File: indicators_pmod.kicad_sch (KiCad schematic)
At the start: 21 parts, among them IC1 ECP5-BGA256

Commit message: rename libraries from luna to cynthion
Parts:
- IC1: footprint luna:lattice_cabga256 -> cynthion:lattice_cabga256
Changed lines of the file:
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@@
       (effects (font (size 1.27 1.27)) (justify right))
     )
-    (property "Footprint" "luna:lattice_cabga256" (id 2) (at -31.75 -35.56 0)
+    (property "Footprint" "cynthion:lattice_cabga256" (id 2) (at -31.75 -35.56 0)
       (effects (font (size 1.27 1.27)) (justify left) hide)
     )

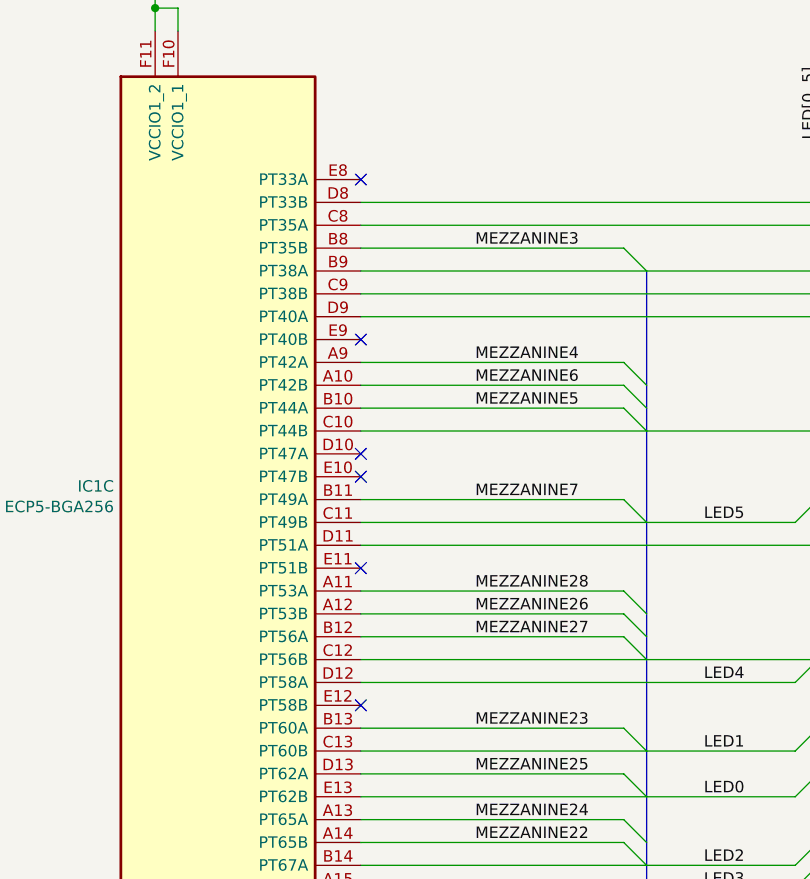
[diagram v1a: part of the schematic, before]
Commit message: Add pseudo-VCCIO and pseudo-GND pins, decoupling
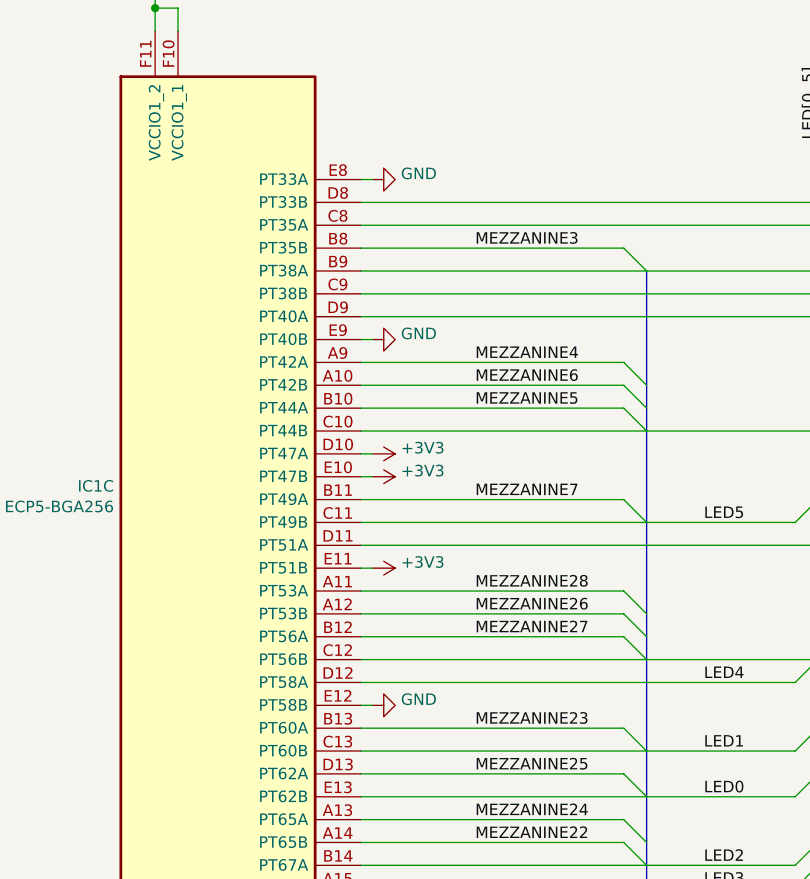
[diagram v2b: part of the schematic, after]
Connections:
- net +3V3: now also IC1.D10 (PT47A), IC1.E10 (PT47B), IC1.E11 (PT51B)
- net GND: now reaches IC1.E12 (PT58B)
- net GND: now also IC1.E8 (PT33A), IC1.E9 (PT40B)
- no-connect marks 6 -> 0
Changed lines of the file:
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@@
   (junction (at 151.765 58.42) (diameter 0) (color 0 0 0 0)
   )
-  (no_connect (at 76.2 93.98))
-  (no_connect (at 76.2 81.28))
-  (no_connect (at 76.2 63.5))
-  (no_connect (at 76.2 106.68))
-  (no_connect (at 76.2 96.52))
-  (no_connect (at 76.2 121.92))
   (bus_entry (at 127 139.7) (size -2.54 2.54)
     (stroke (width 0) (type default) (color 0 0 0 0))
@@
     (stroke (width 0) (type default) (color 0 0 0 0))
   )
+  (wire (pts (xy 76.2 81.28) (xy 77.47 81.28))
+    (stroke (width 0) (type default) (color 0 0 0 0))
+  )
   (wire (pts (xy 129.54 50.8) (xy 139.7 50.8))
     (stroke (width 0) (type default) (color 0 0 0 0))
@@
     (stroke (width 0) (type default) (color 0 0 0 0))
   )
+  (wire (pts (xy 76.2 63.5) (xy 77.47 63.5))
+    (stroke (width 0) (type default) (color 0 0 0 0))
+  )
   (wire (pts (xy 76.2 137.16) (xy 105.41 137.16))
     (stroke (width 0) (type default) (color 0 0 0 0))
   )
+  (wire (pts (xy 77.47 96.52) (xy 76.2 96.52))
+    (stroke (width 0) (type default) (color 0 0 0 0))
+  )
   (wire (pts (xy 177.165 50.8) (xy 179.705 50.8))
     (stroke (width 0) (type default) (color 0 0 0 0))
@@
     (stroke (width 0) (type default) (color 0 0 0 0))
   )
+  (wire (pts (xy 77.47 93.98) (xy 76.2 93.98))
+    (stroke (width 0) (type default) (color 0 0 0 0))
+  )
   (bus (pts (xy 127 60.96) (xy 127 99.06))
     (stroke (width 0) (type default) (color 0 0 0 0))
@@
     (stroke (width 0) (type default) (color 0 0 0 0))
   )
+  (wire (pts (xy 76.2 121.92) (xy 77.47 121.92))
+    (stroke (width 0) (type default) (color 0 0 0 0))
+  )
   (bus (pts (xy 217.17 90.17) (xy 217.17 92.71))
     (stroke (width 0) (type default) (color 0 0 0 0))
@@
   )
   (wire (pts (xy 147.32 55.88) (xy 153.035 55.88))
+    (stroke (width 0) (type default) (color 0 0 0 0))
+  )
+  (wire (pts (xy 76.2 106.68) (xy 77.47 106.68))
     (stroke (width 0) (type default) (color 0 0 0 0))
   )
@@
     )
     (property "Datasheet" "~" (id 3) (at 147.955 37.465 0)
+      (effects (font (size 1.27 1.27)) hide)
+    )
+    (pin "1")
+  )
+  (symbol (lib_id "power:GND") (at 77.47 121.92 90) (unit 1)
+    (in_bom yes) (on_board yes)
+    (property "Reference" "#PWR0232" (id 0) (at 83.82 121.92 0)
+      (effects (font (size 1.27 1.27)) hide)
+    )
+    (property "Value" "GND" (id 1) (at 80.645 121.285 90)
+      (effects (font (size 1.27 1.27)) (justify right))
+    )
+    (property "Footprint" "" (id 2) (at 77.47 121.92 0)
+      (effects (font (size 1.27 1.27)) hide)
+    )
+    (property "Datasheet" "" (id 3) (at 77.47 121.92 0)
       (effects (font (size 1.27 1.27)) hide)
     )
@@
     (pin "1")
   )
+  (symbol (lib_id "power:GND") (at 77.47 63.5 90) (unit 1)
+    (in_bom yes) (on_board yes)
+    (property "Reference" "#PWR0227" (id 0) (at 83.82 63.5 0)
+      (effects (font (size 1.27 1.27)) hide)
+    )
+    (property "Value" "GND" (id 1) (at 80.645 62.865 90)
+      (effects (font (size 1.27 1.27)) (justify right))
+    )
+    (property "Footprint" "" (id 2) (at 77.47 63.5 0)
+      (effects (font (size 1.27 1.27)) hide)
+    )
+    (property "Datasheet" "" (id 3) (at 77.47 63.5 0)
+      (effects (font (size 1.27 1.27)) hide)
+    )
+    (pin "1")
+  )
+  (symbol (lib_id "power:GND") (at 77.47 81.28 90) (unit 1)
+    (in_bom yes) (on_board yes)
+    (property "Reference" "#PWR0228" (id 0) (at 83.82 81.28 0)
+      (effects (font (size 1.27 1.27)) hide)
+    )
+    (property "Value" "GND" (id 1) (at 80.645 80.645 90)
+      (effects (font (size 1.27 1.27)) (justify right))
+    )
+    (property "Footprint" "" (id 2) (at 77.47 81.28 0)
+      (effects (font (size 1.27 1.27)) hide)
+    )
+    (property "Datasheet" "" (id 3) (at 77.47 81.28 0)
+      (effects (font (size 1.27 1.27)) hide)
+    )
+    (pin "1")
+  )
   (symbol (lib_id "Connector:TestPoint") (at 154.305 33.02 0) (mirror y) (unit 1)
     (in_bom no) (on_board yes)
@@
     (pin "8")
   )
+  (symbol (lib_id "power:+3V3") (at 77.47 96.52 270) (unit 1)
+    (in_bom yes) (on_board yes)
+    (property "Reference" "#PWR0224" (id 0) (at 73.66 96.52 0)
+      (effects (font (size 1.27 1.27)) hide)
+    )
+    (property "Value" "+3V3" (id 1) (at 80.645 95.885 90)
+      (effects (font (size 1.27 1.27)) (justify left))
+    )
+    (property "Footprint" "" (id 2) (at 77.47 96.52 0)
+      (effects (font (size 1.27 1.27)) hide)
+    )
+    (property "Datasheet" "" (id 3) (at 77.47 96.52 0)
+      (effects (font (size 1.27 1.27)) hide)
+    )
+    (pin "1")
+  )
   (symbol (lib_id "Device:R_Pack04") (at 195.58 95.25 270) (unit 1)
     (in_bom yes) (on_board yes)
@@
     (pin "8")
   )
+  (symbol (lib_id "power:+3V3") (at 77.47 93.98 270) (unit 1)
+    (in_bom yes) (on_board yes)
+    (property "Reference" "#PWR0231" (id 0) (at 73.66 93.98 0)
+      (effects (font (size 1.27 1.27)) hide)
+    )
+    (property "Value" "+3V3" (id 1) (at 80.645 93.345 90)
+      (effects (font (size 1.27 1.27)) (justify left))
+    )
+    (property "Footprint" "" (id 2) (at 77.47 93.98 0)
+      (effects (font (size 1.27 1.27)) hide)
+    )
+    (property "Datasheet" "" (id 3) (at 77.47 93.98 0)
+      (effects (font (size 1.27 1.27)) hide)
+    )
+    (pin "1")
+  )
+  (symbol (lib_id "power:+3V3") (at 77.47 106.68 270) (unit 1)
+    (in_bom yes) (on_board yes)
+    (property "Reference" "#PWR0225" (id 0) (at 73.66 106.68 0)
+      (effects (font (size 1.27 1.27)) hide)
+    )
+    (property "Value" "+3V3" (id 1) (at 80.645 106.045 90)
+      (effects (font (size 1.27 1.27)) (justify left))
+    )
+    (property "Footprint" "" (id 2) (at 77.47 106.68 0)
+      (effects (font (size 1.27 1.27)) hide)
+    )
+    (property "Datasheet" "" (id 3) (at 77.47 106.68 0)
+      (effects (font (size 1.27 1.27)) hide)
+    )
+    (pin "1")
+  )
 )
